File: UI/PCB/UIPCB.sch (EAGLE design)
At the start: 1 part

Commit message: Circuit for UI
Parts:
- added LED1, LED2, LED3, LED4, LED5: WS2812B, WS2812B:WS2812B
- added S1, S2: (no value), switch-omron:10-XX
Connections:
- new net N$1: LED3.DO, LED4.DI
- new net N$2: LED2.DI, LED4.DO
- new net N$3: LED2.DO, LED5.DI
- new net N$4: LED1.DI, LED5.DO
- new net N$5: LED1.GND, LED2.GND, LED3.GND, LED4.GND, LED5.GND, U$1.GND@1
- new net N$6: LED3.DI, U$1.IO18
- net 5V: now also LED1.VDD, LED2.VDD, LED3.VDD, LED4.VDD, LED5.VDD

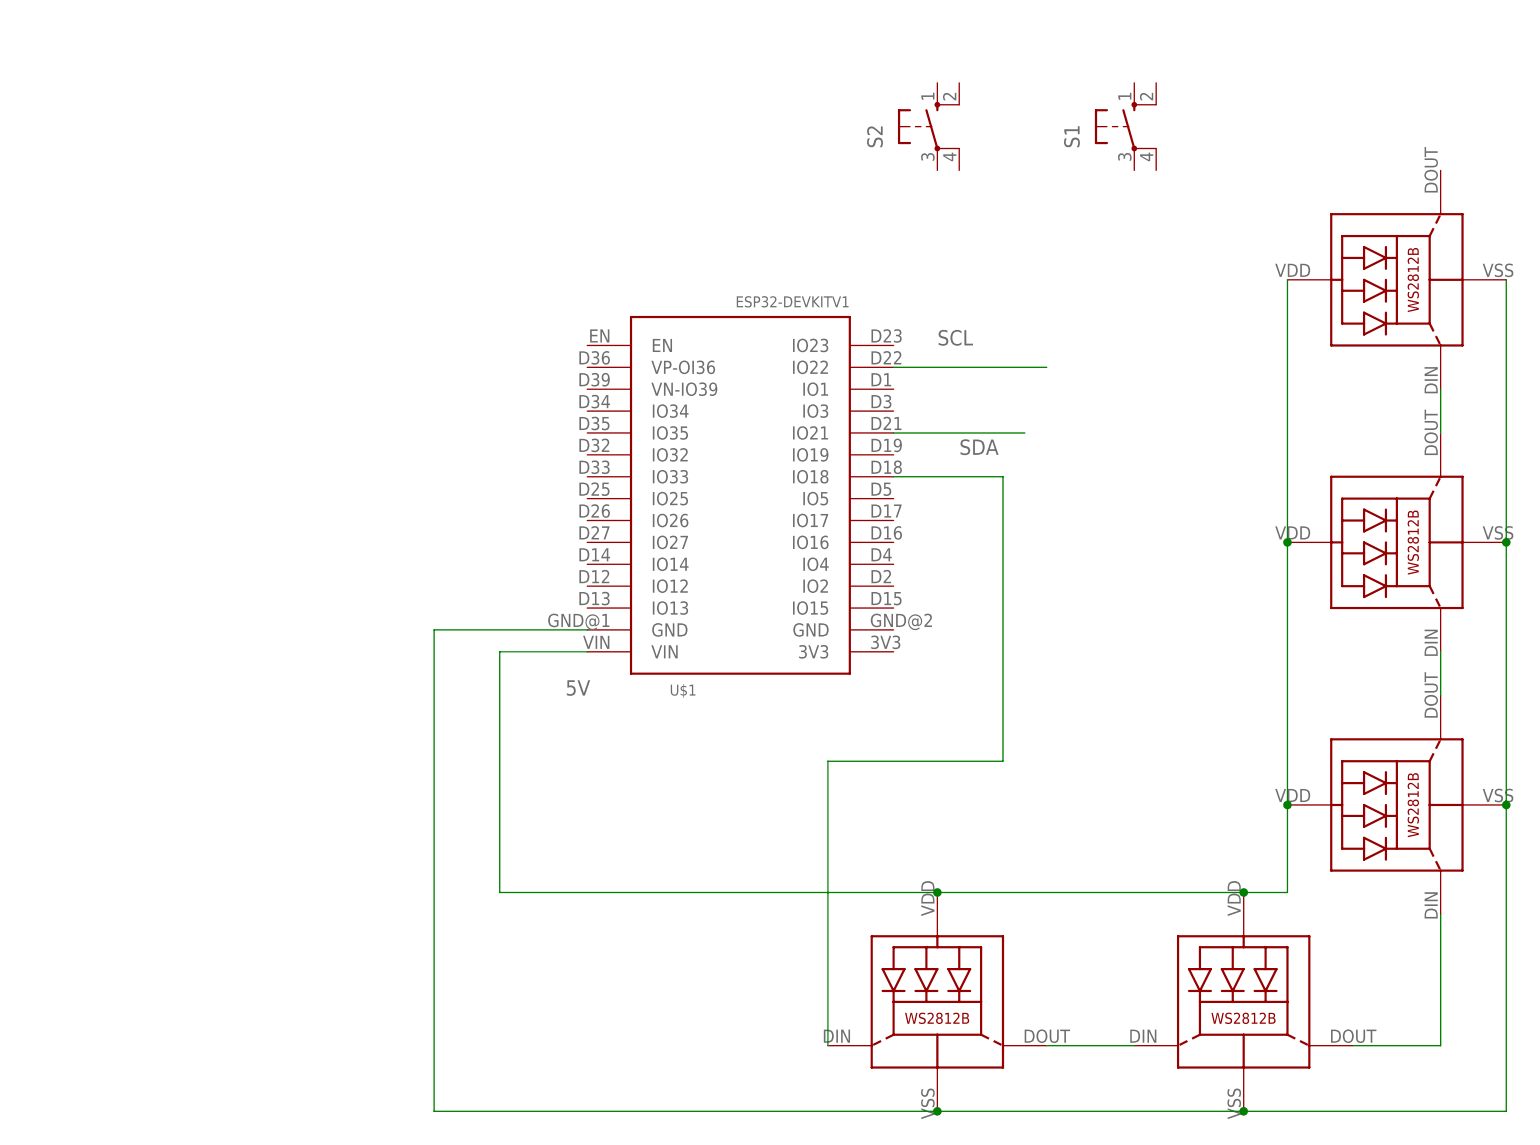
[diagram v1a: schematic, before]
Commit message: added ui board added dashborad basic
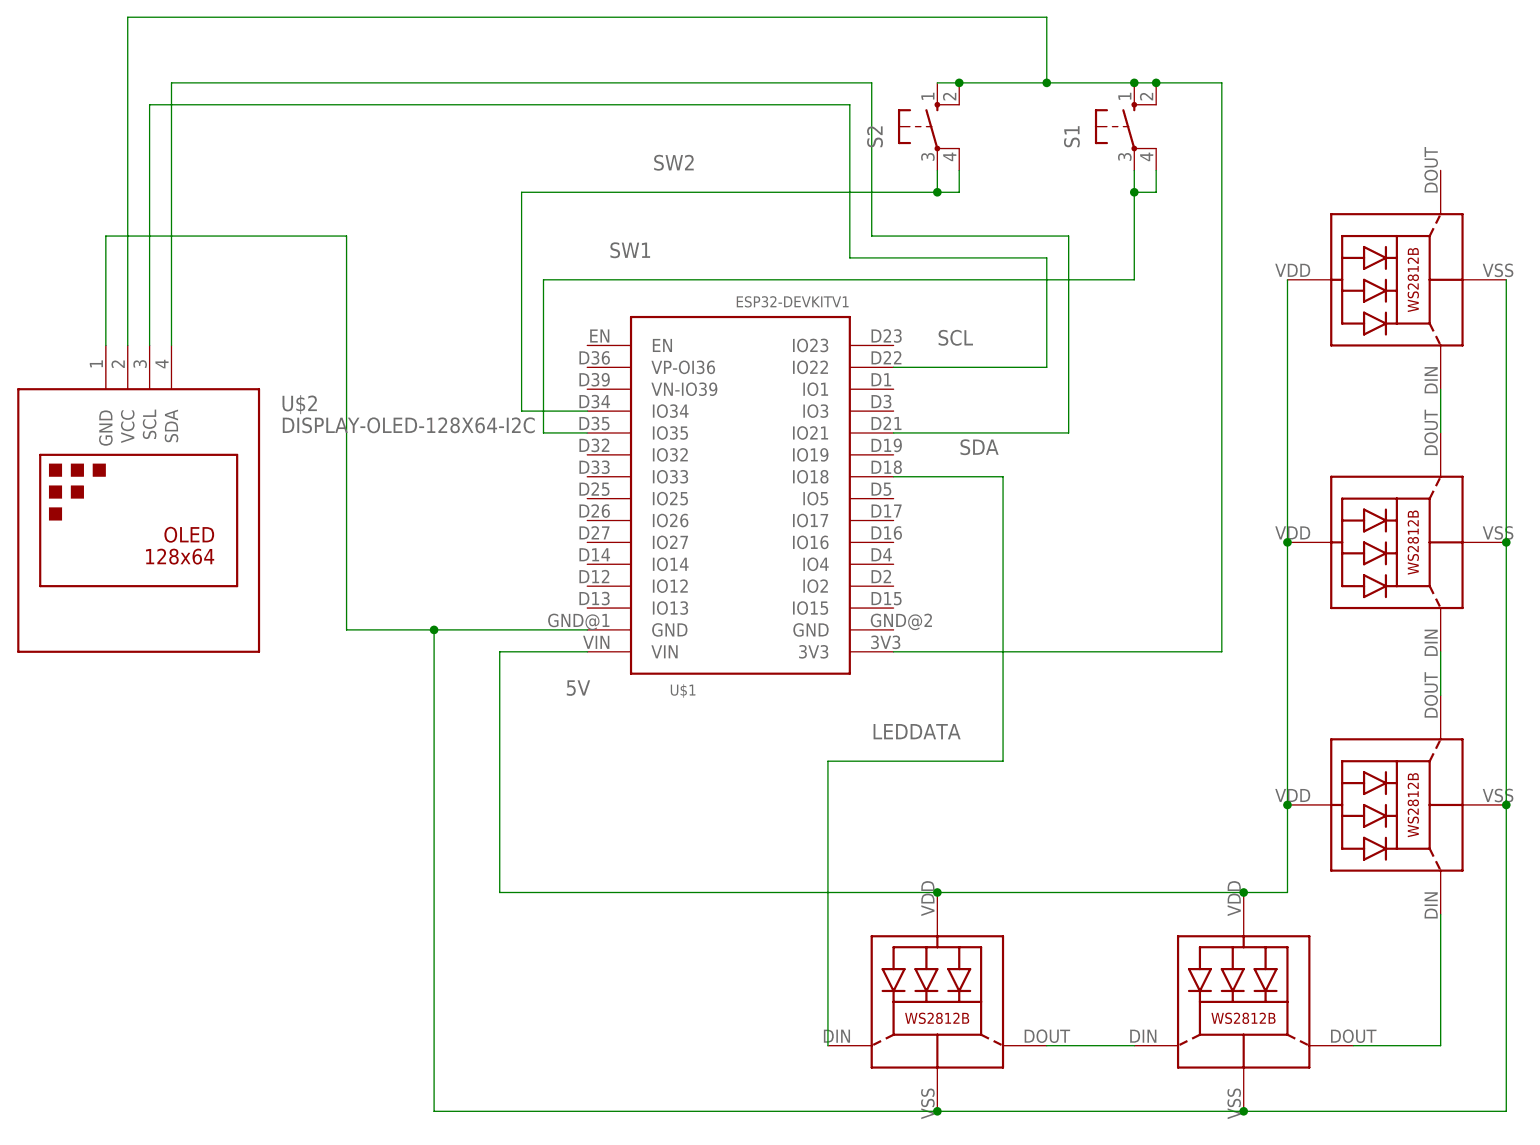
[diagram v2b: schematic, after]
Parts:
- removed LED5: WS2812B, WS2812B:WS2812B
- added LED0: WS2812B, WS2812B:WS2812B
- added U$2: DISPLAY-OLED-128X64-I2C, SSD1306:DISPLAY-OLED-128X64-I2C
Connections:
- removed net N$4 (its old number): LED1.DI, LED5.DO
- removed net N$5: LED1.GND, LED2.GND, LED3.GND, LED4.GND, LED5.GND, U$1.GND@1
- removed net N$6: LED3.DI, U$1.IO18
- new net 3V3: S1.S, S1.S1, S2.S, S2.S1, U$1.3V3, U$2.VCC
- new net GND: LED0.GND, LED1.GND, LED2.GND, LED3.GND, LED4.GND, U$1.GND@1, U$2.GND
- new net LEDDATA: LED0.DI, U$1.IO18
- new net N$1: LED0.DO, LED1.DI
- new net SW1: S1.P, S1.P1, U$1.IO35
- new net SW2: S2.P, S2.P1, U$1.IO34
- net 5V: now also LED0.VDD; no longer LED5.VDD
- net N$2: now also LED1.DO; no longer LED4.DO
- net N$3: now also LED3.DI; no longer LED5.DI
- net SCL: now also U$2.SCL
- net SDA: now also U$2.SDA
